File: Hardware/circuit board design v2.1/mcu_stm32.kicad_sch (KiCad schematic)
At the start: 35 parts, among them J1 Conn_01x02_Male, J4 U.FL-R-SMT-1_10_, J6 Conn_01x02_Male, U1 STM32F446RETx, U10 LAMBDA-9D, U11 2SCR512R_HZG, U2 W25Q64JVSS, U3 SDR08540M3-01, Y1 ECS-80-8-33Q-ADS-TR3

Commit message: Added solder jumpers
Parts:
- added JP1, JP2: SolderJumper_2_Open, Jumper:SolderJumper-2_P1.3mm_Open_TrianglePad1.0x1.5mm, symbol Jumper:SolderJumper_2_Open
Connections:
- net +3.3V: now also JP2.2 (B); no longer R4.2
- net GND: now also JP1.1 (A); no longer D4.1 (K)
- new net: JP2.1 (A), R4.2
- new net: D4.1 (K), JP1.2 (B)
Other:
- moved on the sheet: D4, R3
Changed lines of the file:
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@@
+    (stroke (width 0) (type default) (color 0 0 0 0))
+  )
+  (wire (pts (xy 179.07 127) (xy 179.07 128.27))
     (stroke (width 0) (type default) (color 0 0 0 0))
   )
@@
     (stroke (width 0) (type default) (color 0 0 0 0))
   )
-  (wire (pts (xy 179.07 127) (xy 179.07 120.65))
-    (stroke (width 0) (type default) (color 0 0 0 0))
-  )
   (wire (pts (xy 147.32 46.99) (xy 147.32 49.53))
     (stroke (width 0) (type default) (color 0 0 0 0))
   )
-  (wire (pts (xy 187.96 152.4) (xy 187.96 153.67))
+  (wire (pts (xy 182.88 153.67) (xy 187.96 153.67))
     (stroke (width 0) (type default) (color 0 0 0 0))
   )
@@
     (stroke (width 0) (type default) (color 0 0 0 0))
   )
+  (wire (pts (xy 179.07 120.65) (xy 179.07 121.92))
+    (stroke (width 0) (type default) (color 0 0 0 0))
+  )
   (wire (pts (xy 101.6 137.16) (xy 101.6 135.89))
     (stroke (width 0) (type default) (color 0 0 0 0))
@@
     (stroke (width 0) (type default) (color 0 0 0 0))
   )
-  (wire (pts (xy 179.07 139.7) (xy 179.07 138.43))
+  (wire (pts (xy 195.58 153.67) (xy 203.2 153.67))
     (stroke (width 0) (type default) (color 0 0 0 0))
   )
@@
     (stroke (width 0) (type default) (color 0 0 0 0))
   )
+  (wire (pts (xy 179.07 133.35) (xy 179.07 134.62))
+    (stroke (width 0) (type default) (color 0 0 0 0))
+  )
   (wire (pts (xy 48.26 170.18) (xy 50.8 170.18))
     (stroke (width 0) (type default) (color 0 0 0 0))
@@
     (stroke (width 0) (type default) (color 0 0 0 0))
   )
+  (wire (pts (xy 179.07 142.24) (xy 179.07 143.51))
+    (stroke (width 0) (type default) (color 0 0 0 0))
+  )
   (wire (pts (xy 167.64 57.15) (xy 173.99 57.15))
     (stroke (width 0) (type default) (color 0 0 0 0))
@@
     (stroke (width 0) (type default) (color 0 0 0 0))
   )
-  (wire (pts (xy 179.07 133.35) (xy 179.07 132.08))
-    (stroke (width 0) (type default) (color 0 0 0 0))
-  )
   (wire (pts (xy 194.31 24.13) (xy 194.31 21.59))
     (stroke (width 0) (type default) (color 0 0 0 0))
@@
   )
   (wire (pts (xy 48.26 149.86) (xy 50.8 149.86))
-    (stroke (width 0) (type default) (color 0 0 0 0))
-  )
-  (wire (pts (xy 182.88 153.67) (xy 187.96 153.67))
     (stroke (width 0) (type default) (color 0 0 0 0))
   )
@@
   (hierarchical_label "Mag_Data_Ready" (shape input) (at 127 115.57 180)
     (effects (font (size 1.27 1.27)) (justify right))
+  )
+  (symbol (lib_id "Jumper:SolderJumper_2_Open") (at 191.77 153.67 0) (unit 1)
+    (in_bom yes) (on_board yes) (fields_autoplaced)
+    (property "Reference" "JP2" (id 0) (at 191.77 147.32 0))
+    (property "Value" "SolderJumper_2_Open" (id 1) (at 191.77 149.86 0))
+    (property "Footprint" "Jumper:SolderJumper-2_P1.3mm_Open_TrianglePad1.0x1.5mm" (id 2) (at 191.77 153.67 0)
+      (effects (font (size 1.27 1.27)) hide)
+    )
+    (property "Datasheet" "~" (id 3) (at 191.77 153.67 0)
+      (effects (font (size 1.27 1.27)) hide)
+    )
+    (pin "1")
+    (pin "2")
   )
   (symbol (lib_id "power:+3.3V") (at 62.23 44.45 0) (unit 1)
@@
     (pin "1")
   )
+  (symbol (lib_id "Jumper:SolderJumper_2_Open") (at 179.07 138.43 90) (unit 1)
+    (in_bom yes) (on_board yes) (fields_autoplaced)
+    (property "Reference" "JP1" (id 0) (at 181.61 137.1599 90)
+      (effects (font (size 1.27 1.27)) (justify right))
+    )
+    (property "Value" "SolderJumper_2_Open" (id 1) (at 181.61 139.6999 90)
+      (effects (font (size 1.27 1.27)) (justify right))
+    )
+    (property "Footprint" "Jumper:SolderJumper-2_P1.3mm_Open_TrianglePad1.0x1.5mm" (id 2) (at 179.07 138.43 0)
+      (effects (font (size 1.27 1.27)) hide)
+    )
+    (property "Datasheet" "~" (id 3) (at 179.07 138.43 0)
+      (effects (font (size 1.27 1.27)) hide)
+    )
+    (pin "1")
+    (pin "2")
+  )
   (symbol (lib_id "Device:C_Small") (at 101.6 139.7 0) (unit 1)
     (in_bom yes) (on_board yes) (fields_autoplaced)
@@
     (pin "1")
   )
-  (symbol (lib_id "power:GND") (at 179.07 139.7 0) (unit 1)
-    (in_bom yes) (on_board yes) (fields_autoplaced)
-    (property "Reference" "#PWR0170" (id 0) (at 179.07 146.05 0)
-      (effects (font (size 1.27 1.27)) hide)
-    )
-    (property "Value" "GND" (id 1) (at 179.07 144.78 0))
-    (property "Footprint" "" (id 2) (at 179.07 139.7 0)
-      (effects (font (size 1.27 1.27)) hide)
-    )
-    (property "Datasheet" "" (id 3) (at 179.07 139.7 0)
+  (symbol (lib_id "power:GND") (at 179.07 143.51 0) (unit 1)
+    (in_bom yes) (on_board yes) (fields_autoplaced)
+    (property "Reference" "#PWR0170" (id 0) (at 179.07 149.86 0)
+      (effects (font (size 1.27 1.27)) hide)
+    )
+    (property "Value" "GND" (id 1) (at 179.07 148.59 0))
+    (property "Footprint" "" (id 2) (at 179.07 143.51 0)
+      (effects (font (size 1.27 1.27)) hide)
+    )
+    (property "Datasheet" "" (id 3) (at 179.07 143.51 0)
       (effects (font (size 1.27 1.27)) hide)
     )
@@
     (pin "2")
   )
-  (symbol (lib_id "Components:LED_0603") (at 179.07 135.89 90) (unit 1)
-    (in_bom yes) (on_board yes) (fields_autoplaced)
-    (property "Reference" "D4" (id 0) (at 181.61 134.5564 90)
+  (symbol (lib_id "Components:LED_0603") (at 179.07 130.81 90) (unit 1)
+    (in_bom yes) (on_board yes) (fields_autoplaced)
+    (property "Reference" "D4" (id 0) (at 181.61 129.4764 90)
       (effects (font (size 1.27 1.27)) (justify right))
     )
-    (property "Value" "LED_0603" (id 1) (at 181.61 137.0964 90)
+    (property "Value" "LED_0603" (id 1) (at 181.61 132.0164 90)
       (effects (font (size 1.27 1.27)) (justify right))
     )
-    (property "Footprint" "Components:C_0603_1608Metric" (id 2) (at 179.07 135.89 90)
-      (effects (font (size 1.27 1.27)) hide)
-    )
-    (property "Datasheet" "~" (id 3) (at 179.07 135.89 90)
+    (property "Footprint" "Components:C_0603_1608Metric" (id 2) (at 179.07 130.81 90)
+      (effects (font (size 1.27 1.27)) hide)
+    )
+    (property "Datasheet" "~" (id 3) (at 179.07 130.81 90)
       (effects (font (size 1.27 1.27)) hide)
     )
@@
     (pin "1")
   )
-  (symbol (lib_id "Components:R_0603") (at 179.07 129.54 0) (unit 1)
-    (in_bom yes) (on_board yes) (fields_autoplaced)
-    (property "Reference" "R3" (id 0) (at 181.61 128.2699 0)
-      (effects (font (size 1.27 1.27)) (justify left))
-    )
-    (property "Value" "330" (id 1) (at 181.61 130.8099 0)
-      (effects (font (size 1.27 1.27)) (justify left))
-    )
-    (property "Footprint" "Components:R_0603_1608Metric" (id 2) (at 179.07 129.54 0)
-      (effects (font (size 1.27 1.27)) hide)
-    )
-    (property "Datasheet" "~" (id 3) (at 179.07 129.54 0)
+  (symbol (lib_id "Components:R_0603") (at 179.07 124.46 0) (unit 1)
+    (in_bom yes) (on_board yes) (fields_autoplaced)
+    (property "Reference" "R3" (id 0) (at 181.61 123.1899 0)
+      (effects (font (size 1.27 1.27)) (justify left))
+    )
+    (property "Value" "330" (id 1) (at 181.61 125.7299 0)
+      (effects (font (size 1.27 1.27)) (justify left))
+    )
+    (property "Footprint" "Components:R_0603_1608Metric" (id 2) (at 179.07 124.46 0)
+      (effects (font (size 1.27 1.27)) hide)
+    )
+    (property "Datasheet" "~" (id 3) (at 179.07 124.46 0)
       (effects (font (size 1.27 1.27)) hide)
     )
@@
     (pin "1")
   )
-  (symbol (lib_id "power:+3.3V") (at 187.96 152.4 0) (unit 1)
-    (in_bom yes) (on_board yes) (fields_autoplaced)
-    (property "Reference" "#PWR0158" (id 0) (at 187.96 156.21 0)
-      (effects (font (size 1.27 1.27)) hide)
-    )
-    (property "Value" "+3.3V" (id 1) (at 187.96 147.32 0))
-    (property "Footprint" "" (id 2) (at 187.96 152.4 0)
-      (effects (font (size 1.27 1.27)) hide)
-    )
-    (property "Datasheet" "" (id 3) (at 187.96 152.4 0)
-      (effects (font (size 1.27 1.27)) hide)
-    )
+  (symbol (lib_id "power:+3.3V") (at 203.2 153.67 0) (unit 1)
+    (in_bom yes) (on_board yes) (fields_autoplaced)
+    (property "Reference" "#PWR0158" (id 0) (at 203.2 157.48 0)
+      (effects (font (size 1.27 1.27)) hide)
+    )
+    (property "Value" "+3.3V" (id 1) (at 203.2 148.59 0))
+    (property "Footprint" "" (id 2) (at 203.2 153.67 0)
+      (effects (font (size 1.27 1.27)) hide)
+    )
+    (property "Datasheet" "" (id 3) (at 203.2 153.67 0)
+      (effects (font (size 1.27 1.27)) hide)
+    )

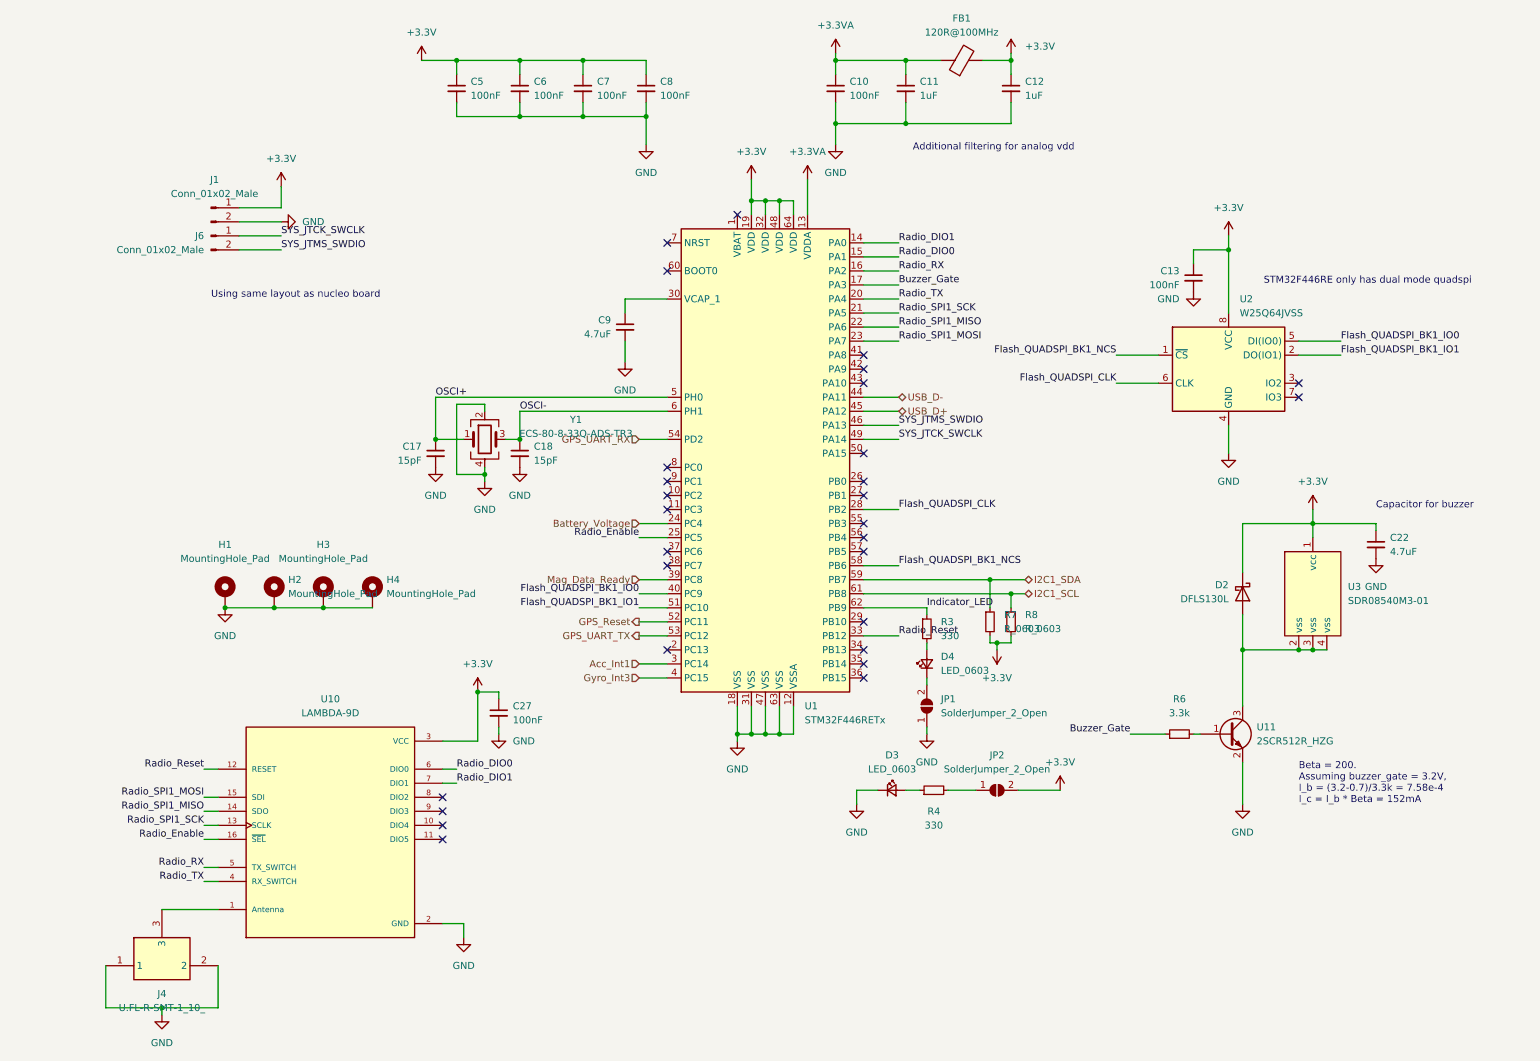
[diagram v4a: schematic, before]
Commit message: PCB V2.1 sent for manufacture
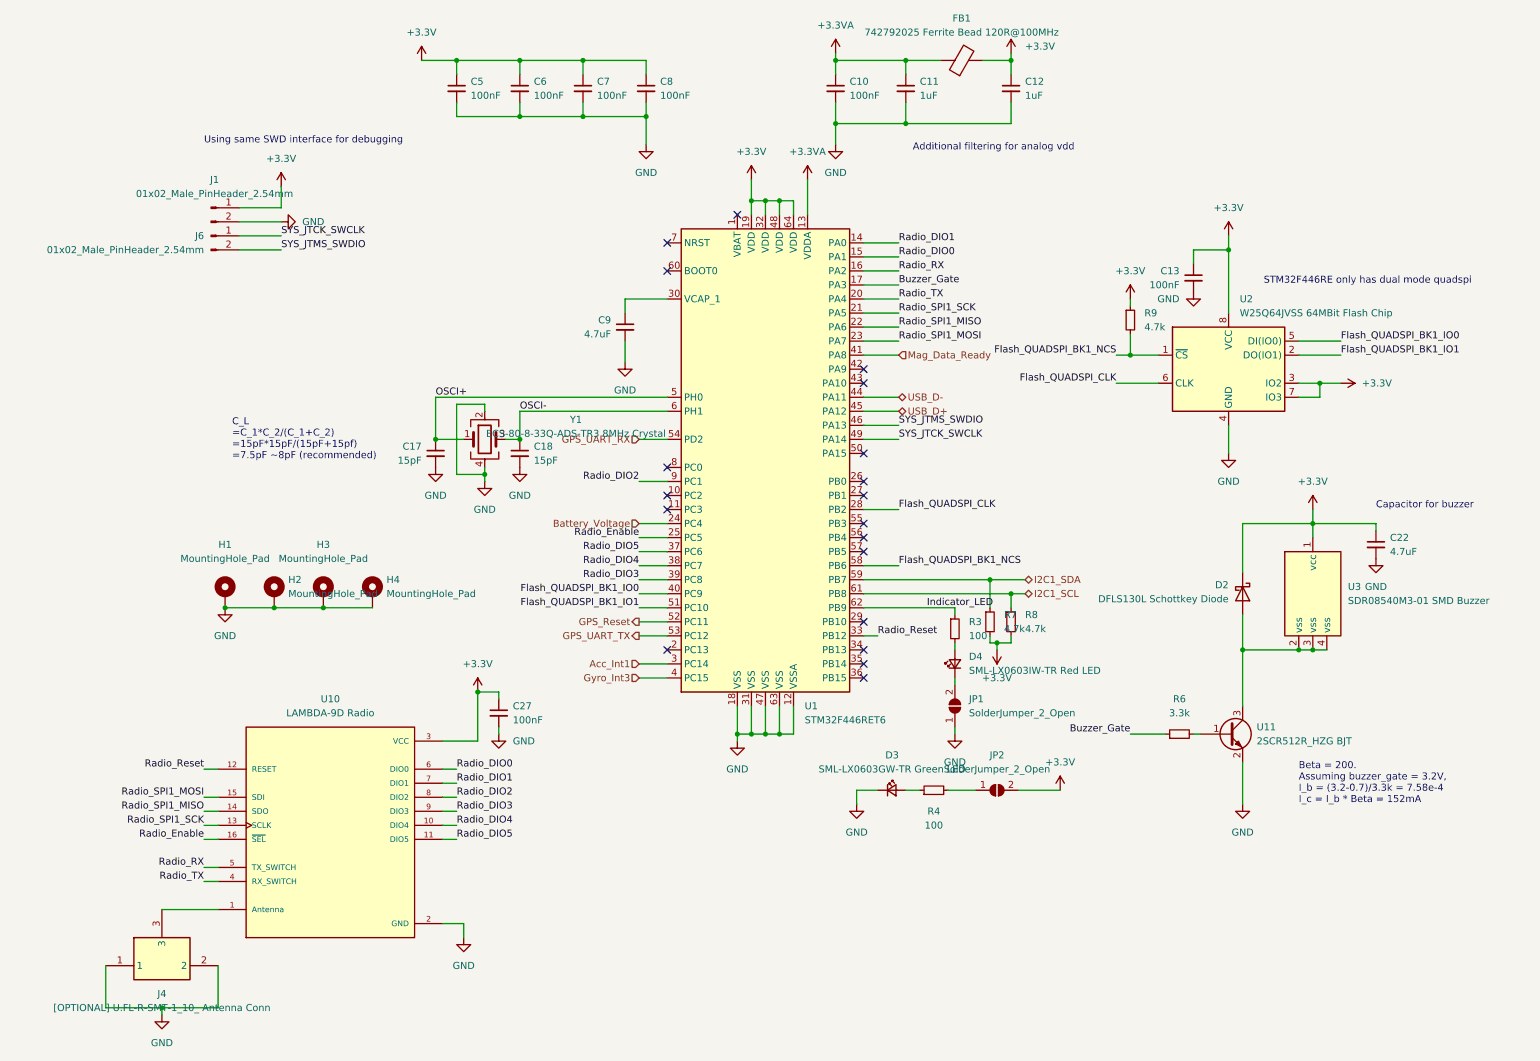
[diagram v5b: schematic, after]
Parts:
- added R9: 4.7k, Components:R_0603_1608Metric, symbol Components:R_0603
- D2: value DFLS130L -> DFLS130L Schottkey Diode
- D3: value LED_0603 -> SML-LX0603GW-TR Green LED
- D4: value LED_0603 -> SML-LX0603IW-TR Red LED
- FB1: value 120R@100MHz -> 742792025 Ferrite Bead 120R@100MHz
- H1, H2, H3, H4, JP1, JP2: now left out of the parts list
- J1, J6: value Conn_01x02_Male -> 01x02_Male_PinHeader_2.54mm
- J4: value U.FL-R-SMT-1_10_ -> [OPTIONAL] U.FL-R-SMT-1_10_ Antenna Conn
- R3, R4: value 330 -> 100
- R7, R8: value R_0603 -> 4.7k
- U1: value STM32F446RETx -> STM32F446RET6
- U10: value LAMBDA-9D -> LAMBDA-9D Radio
- U11: value 2SCR512R_HZG -> 2SCR512R_HZG BJT
- U2: value W25Q64JVSS -> W25Q64JVSS 64MBit Flash Chip
- U3: value SDR08540M3-01 -> SDR08540M3-01 SMD Buzzer
- Y1: value ECS-80-8-33Q-ADS-TR3 -> ECS-80-8-33Q-ADS-TR3 8MHz Crystal
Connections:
- net +3.3V: now also U2.3 (IO2), U2.7 (IO3), R9.1
- net Flash_QUADSPI_BK1_NCS: now also R9.2
- net Mag_Data_Ready: now also U1.41 (PA8); no longer U1.39 (PC8)
- net Radio_DIO4: now reaches U10.10 (DIO4)
- net Radio_DIO4: now also U1.38 (PC7)
- net Radio_DIO5: now reaches U10.11 (DIO5)
- net Radio_DIO5: now also U1.37 (PC6)
- net Radio_DIO2: now reaches U10.8 (DIO2)
- net Radio_DIO2: now also U1.9 (PC1)
- net Radio_DIO3: now reaches U10.9 (DIO3)
- net Radio_DIO3: now also U1.39 (PC8)
- no-connect marks 29 -> 19
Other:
- note added: "C_L =C_1*C_2/(C_1+C_2) =15pF*15pF/(15pF+15pf) =7.5pF ~8pF (recommended)"
- note added: "Using same SWD interface for debugging"
- note removed: "Using same layout as nucleo board"
- moved on the sheet: D4, JP1, R3
